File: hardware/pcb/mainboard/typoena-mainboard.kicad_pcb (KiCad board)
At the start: 4 copper layers, 94 x 45 mm, 95 parts, among them J1 BATTERIE JST-PH, J10 EXTENSION (non monte), J2 BOUTON contact JST-PH, J3 BOUTON LED JST-PH, J4 FPC 24p 0.5mm - PANNEAU, J5 SECOURS DESPI-C579, J6 USB-C CHARGE + PROG, J7 USB-C CLAVIER (hote), J8 microSD, J9 UART PROG, Q1 AO3401A, Q2 2N7002, Q3 2N7002, Q4 Si1308EDL, Q5 2N7002, Q6 2N7002, SW1 QON, SW2 RESET, SW3 BOOT, U1 ESP32-S3-WROOM-1-N16R8, U2 BQ25896RTW, U3 TPS63001DRCR, U4 TPS61023DRL, U5 CH343P

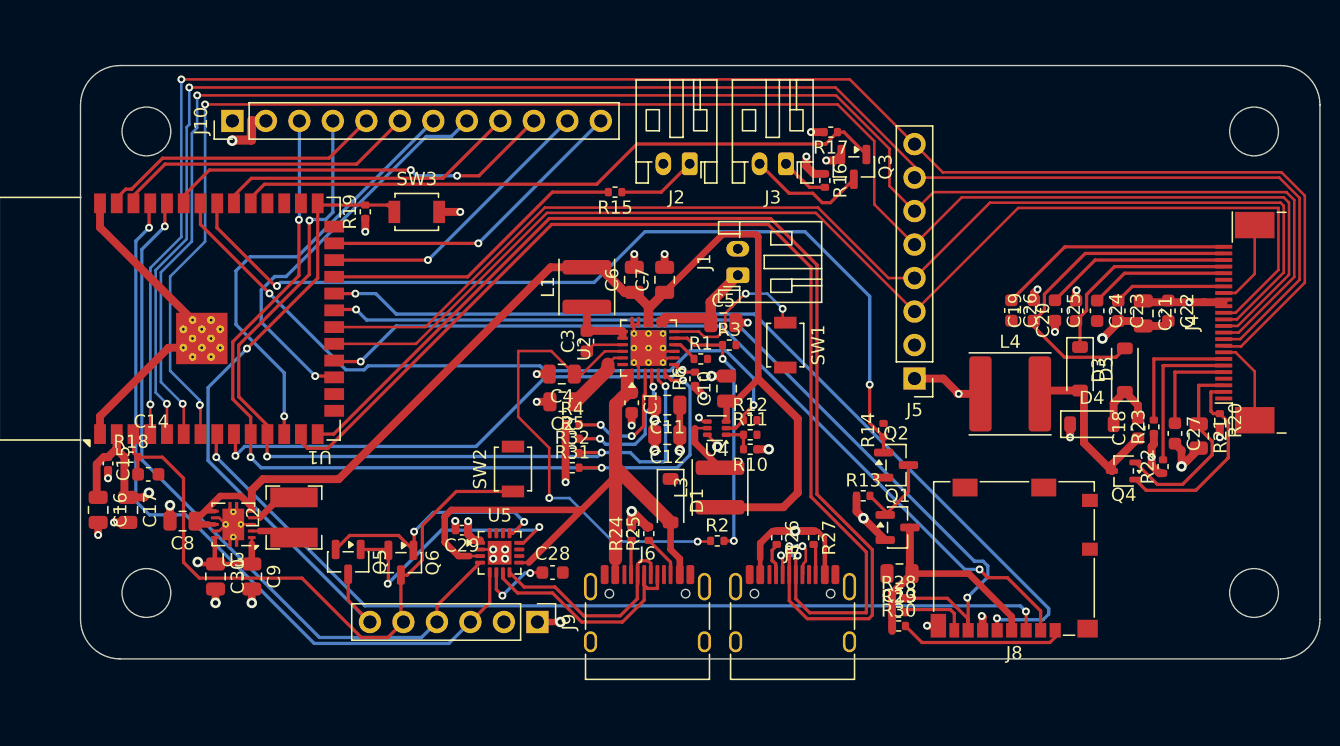
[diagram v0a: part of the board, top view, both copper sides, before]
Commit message: fix(pcb): clear the silkscreen collisions and the In2.Cu ground zone
Reference designators repositioned off every collision: silk_overlap
85 -> 0, silk_over_copper 86 -> 50 as a side effect of preferring
positions clear of pads. Text stays at 1 mm.

GND_in2 dropped. At priority 0 under a board-wide PWR_3V3 it could only
claim 50 mm2 in 47 slivers, and one of them pinched a ground via against
the +3V3 plane at 0.000 mm. In2.Cu is the power layer; ground has its
own solid plane on In1.Cu.

silk_over_copper set to ignore: the fab clips silkscreen off mask
openings. silk_overlap stays a warning, since it catches real damage.

Co-Authored-By: Claude Opus 5 <noreply@anthropic.com>
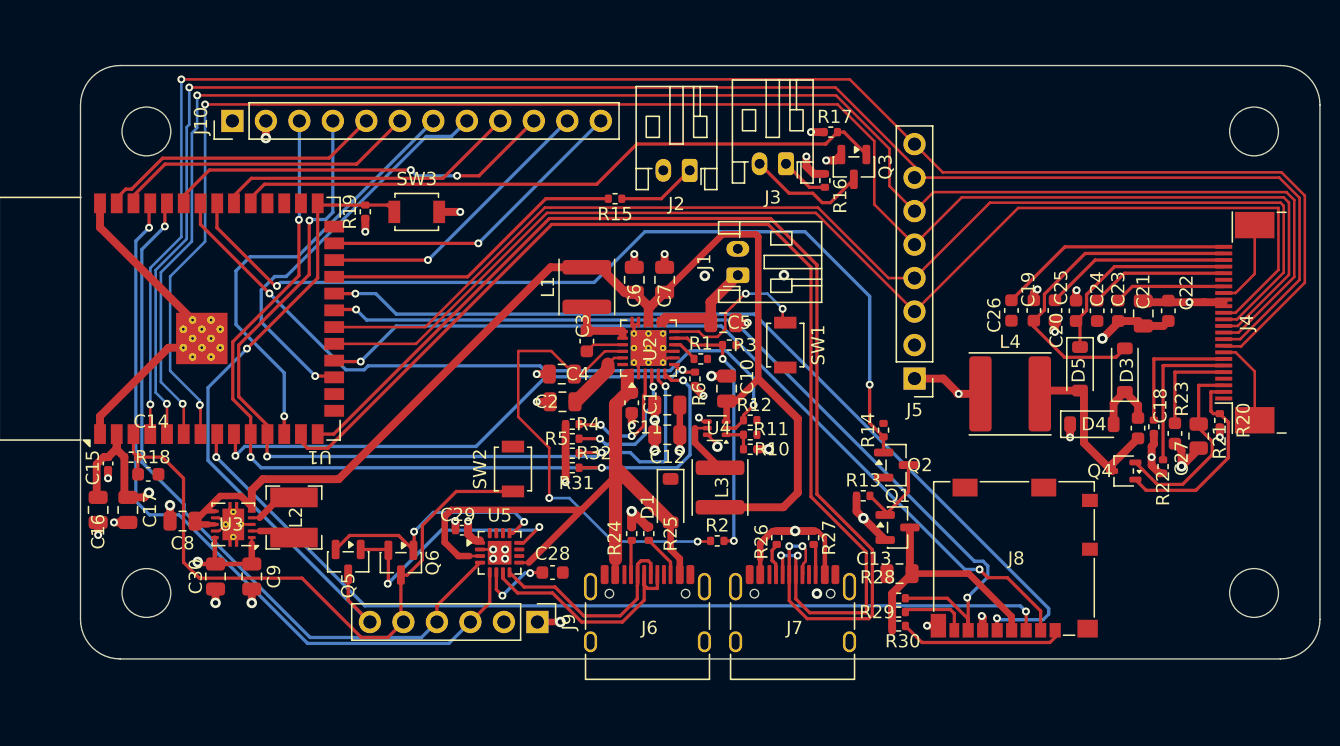
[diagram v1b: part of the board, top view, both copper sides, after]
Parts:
- moved J2 0.50 mm to (86.2, 48.0)
- moved R15 0.50 mm to (80.5, 50.1)
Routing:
- net +3V3: track 57.0 -> 54.3 mm
- net GND: vias 34 -> 37
- removed copper zone on In2.Cu, net GND

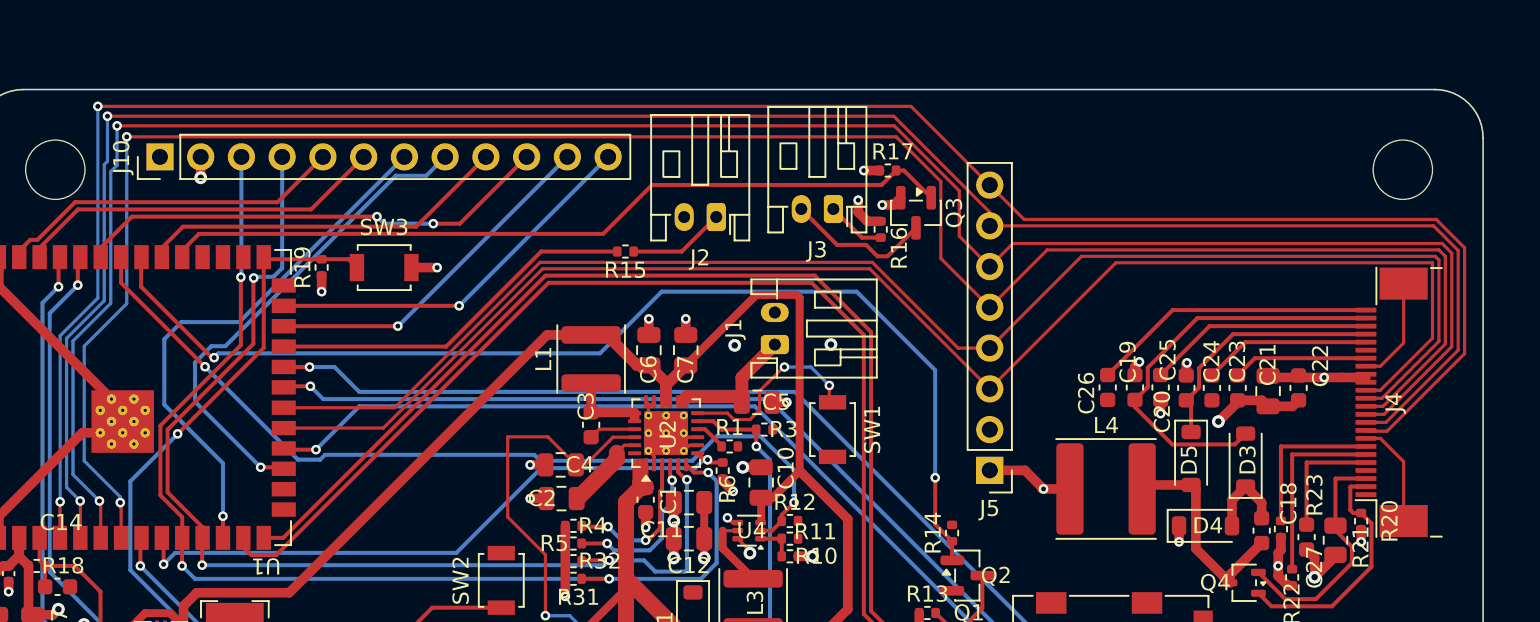
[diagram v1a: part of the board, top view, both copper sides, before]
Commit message: fix(pcb): reroute around the relocated J5 and stitch the loose ground
J5 moves 6.12 mm and J3 0.50 mm; the affected nets are rerouted and the
two references the move pushed into a collision are placed clear again.
Two ground vias tie the last floating GND_surface islands to the plane,
clearing the remaining unconnected item.

Also carries the R10 and R11 value fields, which follow the feedback
divider change in the schematic.

Co-Authored-By: Claude Opus 5 <noreply@anthropic.com>
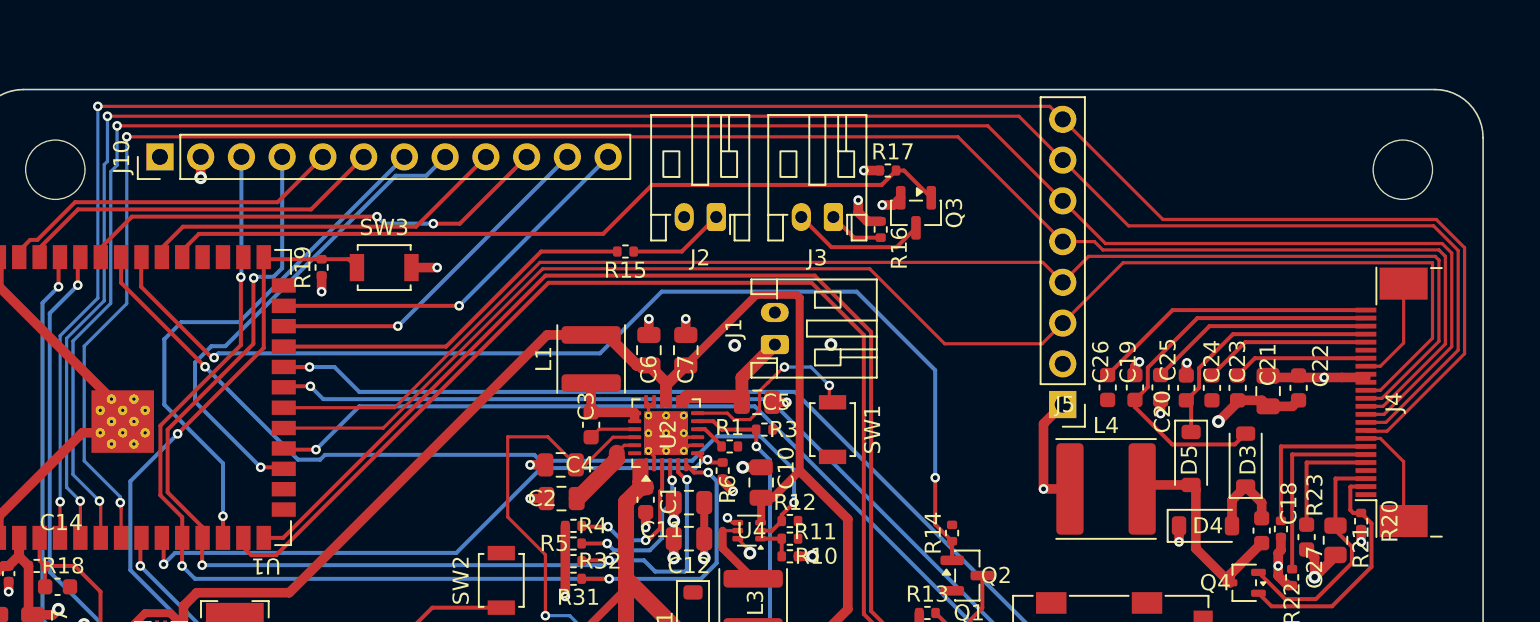
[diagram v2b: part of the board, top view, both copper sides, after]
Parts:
- R10: value 510k 1% -> 56k 1%
- R11: value 68k 1% -> 7.5k 1%
- moved J5 6.12 mm to (107.8, 59.6)
- moved J3 0.50 mm to (93.5, 48.0)
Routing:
- net EPD_CS: track 130.1 -> 124.4 mm
- net EPD_SCK: track 91.5 -> 88.1 mm
- net EPD_DC: track 129.8 -> 127.0 mm
- net EPD_MOSI: track 92.3 -> 89.9 mm
- net +3V3: track 54.3 -> 56.1 mm
- net BTN_LED_K: track 9.11 -> 8.43 mm

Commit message: fix(pcb): turn the VBUS TVS the right way round on both boards
D1 (SMF5.0A, unidirectional) carried Device:D_TVS, KiCad's bidirectional
symbol. Its pins are A1/A2, so no polarity is expressed, ERC has nothing to
reject, and the cathode landed wherever the wire ran — on GND. Plugging in
USB-C would have forward-biased the diode straight across VBUS, shorting the
port it protects.

Both boards now use Device:D_Zener, pin 1 = K, cathode on VBUS. The footprint
is rotated 180° so the symmetric SOD-123 pads keep the same copper: no track
moves, and DRC and unconnected counts are identical before and after.

check_pcb.py gains control H3 — every D<n> footprint must carry K/A pads. It
fails on the boards as they stood and passes 4/4 on the corrected ones.

Co-Authored-By: Claude Opus 5 (1M context) <noreply@anthropic.com>
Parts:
- turned D1 to 90 degrees
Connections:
- D1 pad 1: GND -> VBUS
- D1 pad 2: VBUS -> GND
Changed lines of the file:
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@@
 				)
 			)
-		)		(property "Datasheet" ""
+		)
+		(property "Datasheet" ""
 			(at 0 0 0)
 			(layer "F.Fab")
@@
 				)
 			)
-		)		(property "Datasheet" ""
+		)
+		(property "Datasheet" ""
 			(at 0 0 0)
 			(layer "F.Fab")
@@
 	(footprint "Diode_SMD:D_SOD-123"
 		(layer "F.Cu")
-		(at 84.75 73 -90)
+		(at 84.75 73 90)
 		(descr "SOD-123")
 		(tags "SOD-123")
 		(property "Reference" "D1"
-			(at 0.4659 1.7387 90)
+			(at 0.4659 1.7387 270)
 			(layer "F.SilkS")
 			(effects
@@
 		)
 		(property "Value" "SMF5.0A"
-			(at 0 2.1 90)
+			(at 0 2.1 270)
 			(layer "F.Fab")
 			(effects
@@
 		)
 		(property "Datasheet" ""
-			(at 0 0 270)
+			(at 0 0 90)
 			(unlocked yes)
 			(layer "F.Fab")
@@
 		)
 		(property "Description" ""
-			(at 0 0 270)
+			(at 0 0 90)
 			(unlocked yes)
 			(layer "F.Fab")
@@
 		)
 		(property "LCSC" "C284108"
-			(at 0 0 270)
+			(at 0 0 90)
 			(unlocked yes)
 			(layer "F.Fab")
@@
 		)
 		(property "MPN" "SMF5.0A"
-			(at 0 0 270)
+			(at 0 0 90)
 			(unlocked yes)
 			(layer "F.Fab")
@@
 		(duplicate_pad_numbers_are_jumpers no)
 		(fp_line
-			(start -2.36 1)
-			(end 1.65 1)
+			(start -2.36 -1)
+			(end 1.65 -1)
 			(stroke
 				(width 0.12)
@@
 		)
 		(fp_line
-			(start -2.36 -1)
-			(end 1.65 -1)
+			(start -2.36 1)
+			(end 1.65 1)
 			(stroke
 				(width 0.12)
@@
 		)
 		(fp_line
-			(start 2.35 1.15)
-			(end -2.35 1.15)
+			(start 2.35 -1.15)
+			(end 2.35 1.15)
 			(stroke
 				(width 0.05)
@@
 		(fp_line
 			(start -2.35 -1.15)
-			(end -2.35 1.15)
+			(end 2.35 -1.15)
 			(stroke
 				(width 0.05)
@@
 		(fp_line
 			(start -2.35 -1.15)
-			(end 2.35 -1.15)
+			(end -2.35 1.15)
 			(stroke
 				(width 0.05)
@@
 		)
 		(fp_line
-			(start 2.35 -1.15)
-			(end 2.35 1.15)
+			(start 2.35 1.15)
+			(end -2.35 1.15)
 			(stroke
 				(width 0.05)
@@
 		)
 		(fp_line
-			(start -1.4 0.9)
-			(end -1.4 -0.9)
+			(start 1.4 -0.9)
+			(end 1.4 0.9)
 			(stroke
 				(width 0.1)
@@
 		)
 		(fp_line
-			(start 1.4 0.9)
-			(end -1.4 0.9)
+			(start -1.4 -0.9)
+			(end 1.4 -0.9)
 			(stroke
 				(width 0.1)
@@
 		)
 		(fp_line
-			(start 0.25 0.4)
-			(end -0.35 0)
+			(start 0.25 -0.4)
+			(end 0.25 0.4)
 			(stroke
 				(width 0.1)
@@
 		)
 		(fp_line
-			(start -0.75 0)
-			(end -0.35 0)
+			(start 0.25 0)
+			(end 0.75 0)
 			(stroke
 				(width 0.1)
@@
 		(fp_line
 			(start -0.35 0)
-			(end -0.35 0.55)
+			(end -0.35 -0.55)
 			(stroke
 				(width 0.1)
@@
 		(fp_line
 			(start -0.35 0)
-			(end -0.35 -0.55)
+			(end -0.35 0.55)
 			(stroke
 				(width 0.1)
@@
 		)
 		(fp_line
-			(start 0.25 0)
-			(end 0.75 0)
+			(start -0.75 0)
+			(end -0.35 0)
 			(stroke
 				(width 0.1)
@@
 		)
 		(fp_line
-			(start 0.25 -0.4)
-			(end 0.25 0.4)
+			(start 0.25 0.4)
+			(end -0.35 0)
 			(stroke
 				(width 0.1)
@@
 		)
 		(fp_line
-			(start -1.4 -0.9)
-			(end 1.4 -0.9)
+			(start 1.4 0.9)
+			(end -1.4 0.9)
 			(stroke
 				(width 0.1)
@@
 		)
 		(fp_line
-			(start 1.4 -0.9)
-			(end 1.4 0.9)
+			(start -1.4 0.9)
+			(end -1.4 -0.9)
 			(stroke
 				(width 0.1)
@@
 		)
 		(fp_text user "${REFERENCE}"
-			(at 0 -2 90)
+			(at 0 -2 270)
 			(layer "F.Fab")
 			(effects
@@
 		)
 		(pad "1" smd roundrect
-			(at -1.65 0 270)
+			(at -1.65 0 90)
 			(size 0.9 1.2)
 			(layers "F.Cu" "F.Mask" "F.Paste")
 			(roundrect_rratio 0.25)
-			(net "GND")
-			(pinfunction "A1_1")
+			(net "VBUS")
+			(pinfunction "K_1")
 			(pintype "passive")
 		)
 		(pad "2" smd roundrect
-			(at 1.65 0 270)
+			(at 1.65 0 90)
 			(size 0.9 1.2)
 			(layers "F.Cu" "F.Mask" "F.Paste")
 			(roundrect_rratio 0.25)
-			(net "VBUS")
-			(pinfunction "A2_2")
+			(net "GND")
+			(pinfunction "A_2")
 			(pintype "passive")
 		)
@@
 		(tags "Through hole pin header THT 1x08 2.54mm single row")
 		(property "Reference" "J5"
-			(at -0.1500 0.0000 0)
+			(at -0.15 0 0)
 			(layer "F.SilkS")
 			(effects
